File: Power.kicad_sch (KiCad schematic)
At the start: 30 parts

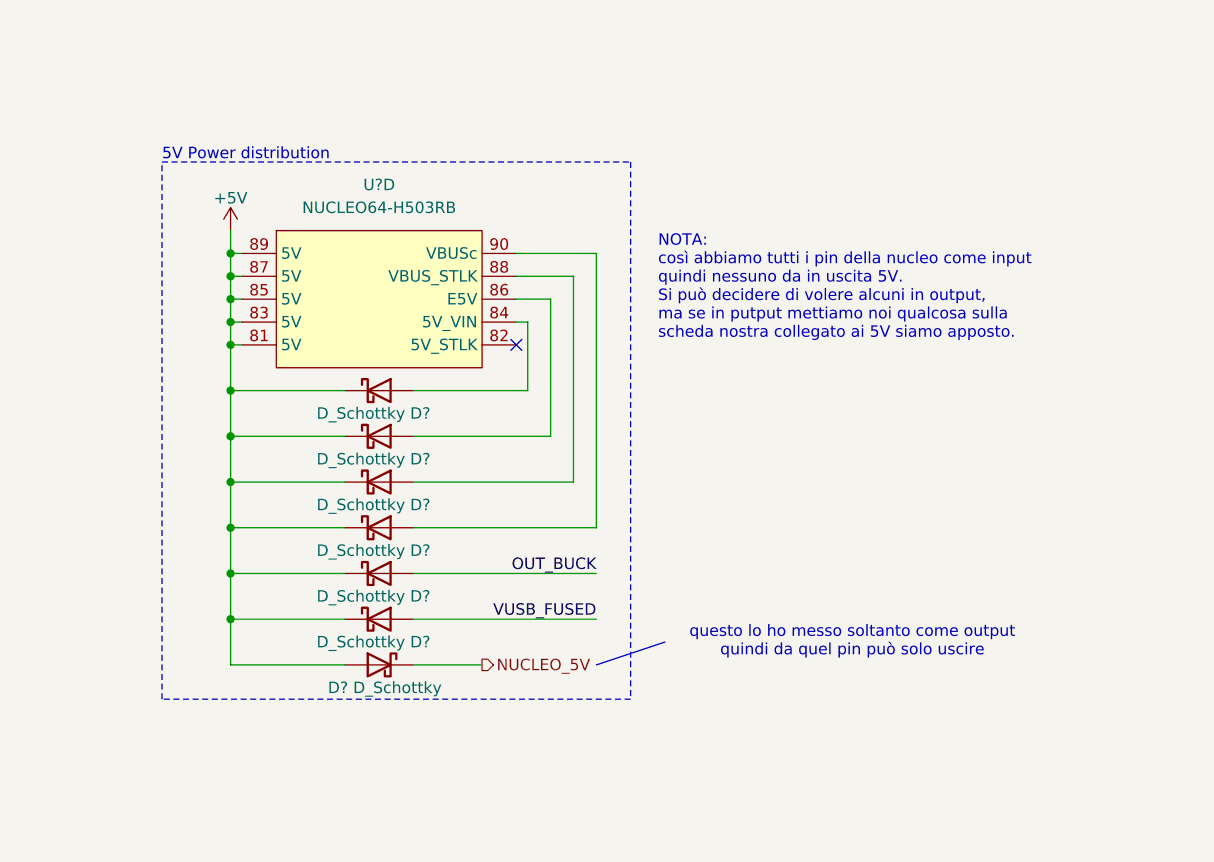
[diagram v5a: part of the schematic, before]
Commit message: Changed the grounding of the opto-coupled power stage + Added UI connectors + Removed a Diode on the Power Sheet (Fixes #3)
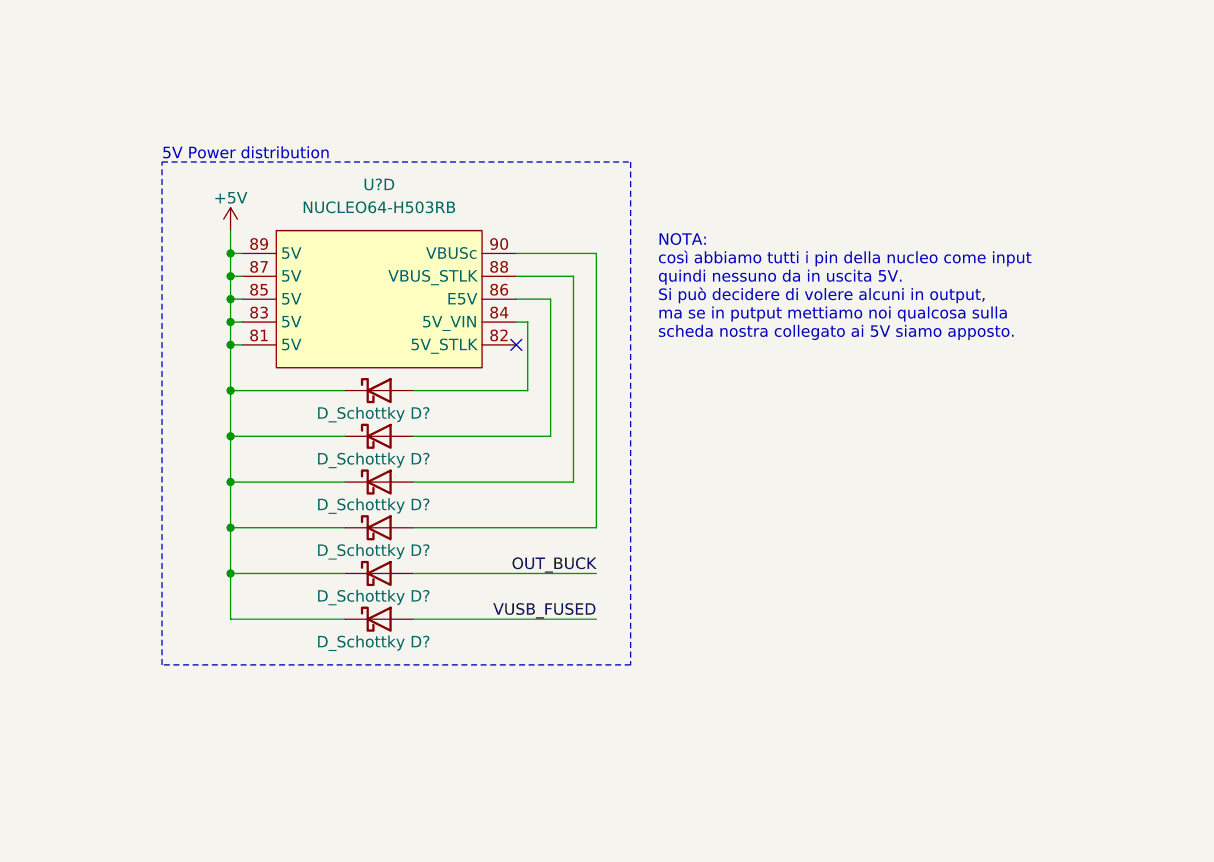
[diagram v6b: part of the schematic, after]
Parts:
- removed D?: D_Schottky, symbol Device:D_Schottky
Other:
- note removed: "questo lo ho messo soltanto come output quindi da quel pin può solo uscire"
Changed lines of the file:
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@@
 	(rectangle
 		(start 180.34 102.87)
-		(end 232.41 162.56)
+		(end 232.41 158.75)
 		(stroke
 			(width 0)
@@
 		)
 	)
-	(text "questo lo ho messo soltanto come output\nquindi da quel pin può solo uscire"
-		(exclude_from_sim no)
-		(at 257.048 156.21 0)
-		(effects
-			(font
-				(size 1.27 1.27)
-			)
-		)
-	)
 	(text "5V Power distribution"
 		(exclude_from_sim no)
@@
 	)
 	(junction
-		(at 187.96 153.67)
-		(diameter 0)
-		(color 0 0 0 0)
-	)
-	(junction
 		(at 161.29 33.02)
 		(diameter 0)
@@
 	(wire
 		(pts
-			(xy 208.28 158.75) (xy 215.9 158.75)
-		)
-		(stroke
-			(width 0)
-			(type default)
-		)
-	)
-	(wire
-		(pts
 			(xy 46.99 167.64) (xy 46.99 165.1)
 		)
@@
 	(wire
 		(pts
-			(xy 200.66 158.75) (xy 187.96 158.75)
-		)
-		(stroke
-			(width 0)
-			(type default)
-		)
-	)
-	(wire
-		(pts
 			(xy 95.25 41.91) (xy 95.25 43.18)
 		)
@@
 	(wire
 		(pts
+			(xy 219.71 115.57) (xy 226.06 115.57)
+		)
+		(stroke
+			(width 0)
+			(type default)
+		)
+	)
+	(wire
+		(pts
 			(xy 187.96 133.35) (xy 200.66 133.35)
 		)
@@
 	(wire
 		(pts
-			(xy 219.71 115.57) (xy 226.06 115.57)
-		)
-		(stroke
-			(width 0)
-			(type default)
-		)
-	)
-	(wire
-		(pts
 			(xy 191.77 33.02) (xy 207.01 33.02)
 		)
@@
 	(wire
 		(pts
-			(xy 187.96 158.75) (xy 187.96 153.67)
-		)
-		(stroke
-			(width 0)
-			(type default)
-		)
-	)
-	(wire
-		(pts
 			(xy 95.25 44.45) (xy 95.25 43.18)
 		)
@@
 		)
 	)
-	(polyline
-		(pts
-			(xy 228.6 158.75) (xy 236.22 156.21)
-		)
-		(stroke
-			(width 0)
-			(type default)
-		)
-	)
 	(wire
 		(pts
@@
 		)
 	)
-	(hierarchical_label "NUCLEO_5V"
-		(shape output)
-		(at 215.9 158.75 0)
-		(effects
-			(font
-				(size 1.27 1.27)
-			)
-			(justify left)
-		)
-	)
 	(hierarchical_label "NUCLEO_3V3"
 		(shape input)
@@
 	)
 	(symbol
-		(lib_id "Device:D_Schottky")
-		(at 204.47 158.75 0)
-		(mirror y)
-		(unit 1)
-		(exclude_from_sim no)
-		(in_bom yes)
-		(on_board yes)
-		(dnp no)
-		(property "Reference" "D?"
-			(at 199.898 161.29 0)
-			(effects
-				(font
-					(size 1.27 1.27)
-				)
-			)
-		)
-		(property "Value" "D_Schottky"
-			(at 206.502 161.29 0)
-			(effects
-				(font
-					(size 1.27 1.27)
-				)
-			)
-		)
-		(property "Footprint" ""
-			(at 204.47 158.75 0)
-			(effects
-				(font
-					(size 1.27 1.27)
-				)
-				(hide yes)
-			)
-		)
-		(property "Datasheet" "~"
-			(at 204.47 158.75 0)
-			(effects
-				(font
-					(size 1.27 1.27)
-				)
-				(hide yes)
-			)
-		)
-		(property "Description" "Schottky diode"
-			(at 204.47 158.75 0)
-			(effects
-				(font
-					(size 1.27 1.27)
-				)
-				(hide yes)
-			)
-		)
-		(pin "2"
-		)
-		(pin "1"
-		)
-		(instances
-			(project "Educational-Board_MainBoard"
-				(path "/835b4df9-7d62-45f4-81d2-5a64fbc86f3c/a1b70c1b-93fd-432d-b3bf-990581065c7c"
-					(reference "D?")
-					(unit 1)
-				)
-			)
-		)
-	)
-	(symbol
 		(lib_id "power:GND")
 		(at 238.76 46.99 0)
@@
 		(dnp no)
 		(fields_autoplaced yes)
-		(property "Reference" "#PWR030"
+		(property "Reference" "#PWR?"
 			(at 187.96 114.3 0)
 			(effects
@@
 			(project "Educational-Board_MainBoard"
 				(path "/835b4df9-7d62-45f4-81d2-5a64fbc86f3c/a1b70c1b-93fd-432d-b3bf-990581065c7c"
-					(reference "#PWR030")
+					(reference "#PWR?")
 					(unit 1)
 				)

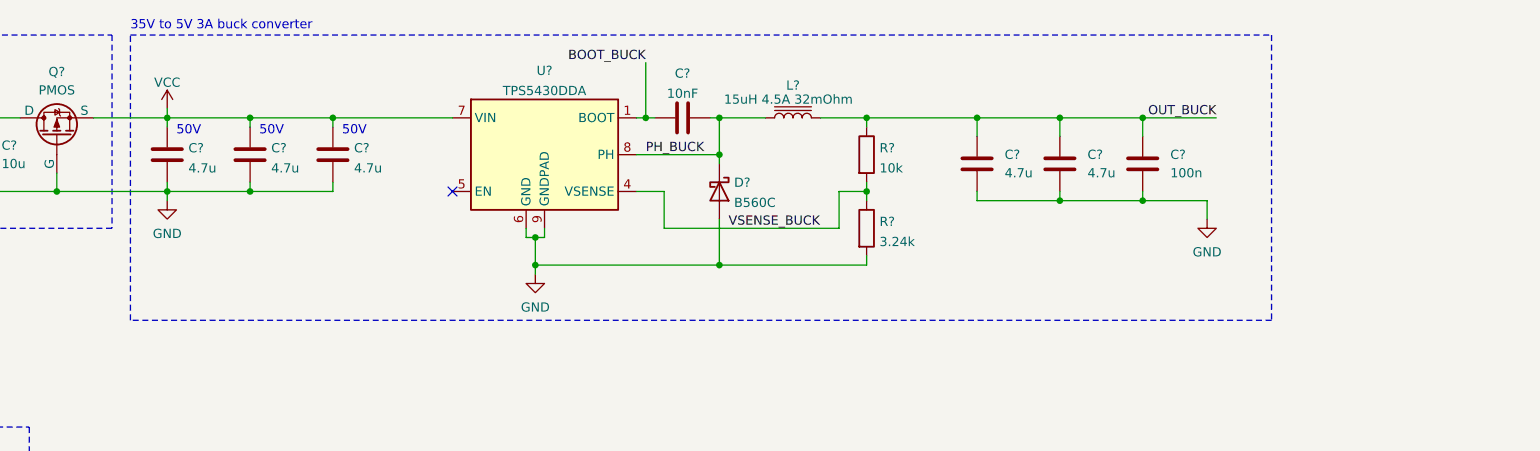
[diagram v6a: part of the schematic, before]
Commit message: Completated the Power Schema + Added Shunts resistors with OP Amp + Connected the RGB Connector to the BUCK (Fixes #5)
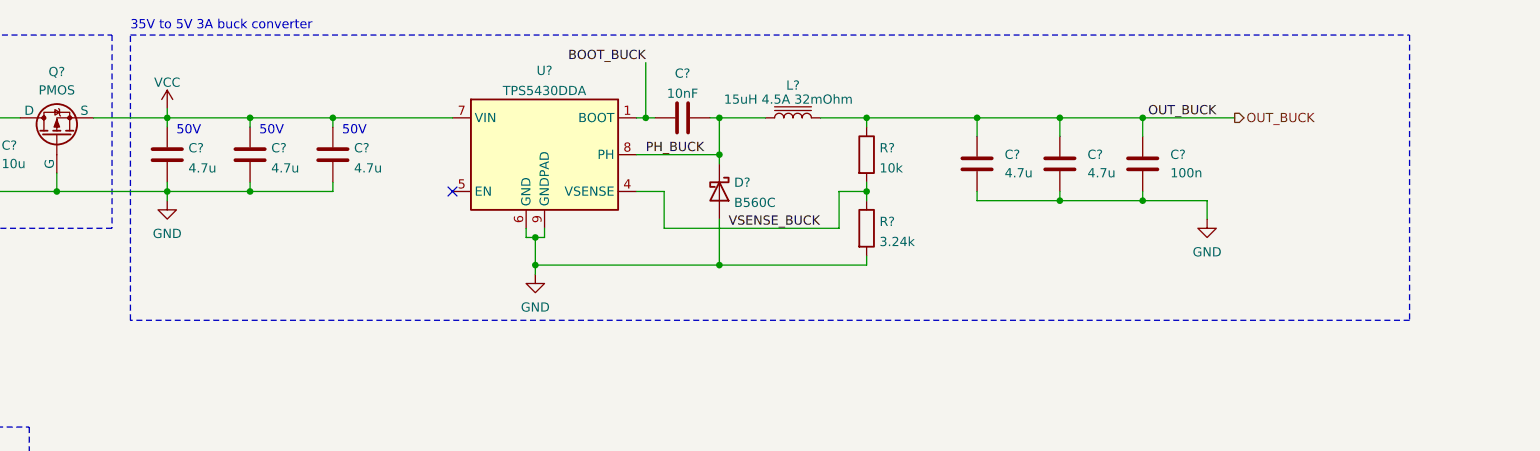
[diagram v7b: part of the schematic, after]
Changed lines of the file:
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@@
 	(rectangle
 		(start 90.17 21.59)
-		(end 247.65 60.96)
+		(end 266.7 60.96)
 		(stroke
 			(width 0)
@@
 	(wire
 		(pts
-			(xy 240.03 33.02) (xy 229.87 33.02)
+			(xy 229.87 33.02) (xy 242.57 33.02)
 		)
 		(stroke
@@
 		)
 	)
+	(hierarchical_label "OUT_BUCK"
+		(shape output)
+		(at 242.57 33.02 0)
+		(effects
+			(font
+				(size 1.27 1.27)
+			)
+			(justify left)
+		)
+	)
 	(hierarchical_label "NUCLEO_VDD"
 		(shape input)
@@
 		(dnp no)
 		(fields_autoplaced yes)
-		(property "Reference" "#PWR?"
+		(property "Reference" "#PWR0106"
 			(at 50.8 87.63 0)
 			(effects
@@
 			(project ""
 				(path "/835b4df9-7d62-45f4-81d2-5a64fbc86f3c/a1b70c1b-93fd-432d-b3bf-990581065c7c"
-					(reference "#PWR?")
+					(reference "#PWR0106")
 					(unit 1)
 				)
@@
 		(dnp no)
 		(fields_autoplaced yes)
-		(property "Reference" "#PWR?"
+		(property "Reference" "#PWR0107"
 			(at 85.09 161.29 0)
 			(effects
@@
 			(project "Educational-Board_MainBoard"
 				(path "/835b4df9-7d62-45f4-81d2-5a64fbc86f3c/a1b70c1b-93fd-432d-b3bf-990581065c7c"
-					(reference "#PWR?")
+					(reference "#PWR0107")
 					(unit 1)
 				)
@@
 		(dnp no)
 		(fields_autoplaced yes)
-		(property "Reference" "#PWR?"
+		(property "Reference" "#PWR0104"
 			(at 238.76 53.34 0)
 			(effects
@@
 			(project "Educational-Board_MainBoard"
 				(path "/835b4df9-7d62-45f4-81d2-5a64fbc86f3c/a1b70c1b-93fd-432d-b3bf-990581065c7c"
-					(reference "#PWR?")
+					(reference "#PWR0104")
 					(unit 1)
 				)
@@
 		(dnp no)
 		(fields_autoplaced yes)
-		(property "Reference" "#PWR?"
+		(property "Reference" "#PWR0105"
 			(at 187.96 114.3 0)
 			(effects
@@
 			(project "Educational-Board_MainBoard"
 				(path "/835b4df9-7d62-45f4-81d2-5a64fbc86f3c/a1b70c1b-93fd-432d-b3bf-990581065c7c"
-					(reference "#PWR?")
+					(reference "#PWR0105")
 					(unit 1)
 				)
@@
 		(dnp no)
 		(fields_autoplaced yes)
-		(property "Reference" "#PWR?"
+		(property "Reference" "#PWR0110"
 			(at 33.02 190.5 0)
 			(effects
@@
 			(project "Educational-Board_MainBoard"
 				(path "/835b4df9-7d62-45f4-81d2-5a64fbc86f3c/a1b70c1b-93fd-432d-b3bf-990581065c7c"
-					(reference "#PWR?")
+					(reference "#PWR0110")
 					(unit 1)
 				)
@@
 		(dnp no)
 		(fields_autoplaced yes)
-		(property "Reference" "#PWR?"
+		(property "Reference" "#PWR0109"
 			(at 62.23 171.45 0)
 			(effects
@@
 			(project "Educational-Board_MainBoard"
 				(path "/835b4df9-7d62-45f4-81d2-5a64fbc86f3c/a1b70c1b-93fd-432d-b3bf-990581065c7c"
-					(reference "#PWR?")
+					(reference "#PWR0109")
 					(unit 1)
 				)
@@
 		(dnp no)
 		(fields_autoplaced yes)
-		(property "Reference" "#PWR?"
+		(property "Reference" "#PWR0101"
 			(at 146.05 60.96 0)
 			(effects
@@
 			(project "Educational-Board_MainBoard"
 				(path "/835b4df9-7d62-45f4-81d2-5a64fbc86f3c/a1b70c1b-93fd-432d-b3bf-990581065c7c"
-					(reference "#PWR?")
+					(reference "#PWR0101")
 					(unit 1)
 				)
@@
 		(dnp no)
 		(fields_autoplaced yes)
-		(property "Reference" "#PWR?"
+		(property "Reference" "#PWR0103"
 			(at 95.25 35.56 0)
 			(effects
@@
 			(project "Educational-Board_MainBoard"
 				(path "/835b4df9-7d62-45f4-81d2-5a64fbc86f3c/a1b70c1b-93fd-432d-b3bf-990581065c7c"
-					(reference "#PWR?")
+					(reference "#PWR0103")
 					(unit 1)
 				)
@@
 		(dnp no)
 		(fields_autoplaced yes)
-		(property "Reference" "#PWR?"
+		(property "Reference" "#PWR0102"
 			(at 95.25 50.8 0)
 			(effects
@@
 			(project "Educational-Board_MainBoard"
 				(path "/835b4df9-7d62-45f4-81d2-5a64fbc86f3c/a1b70c1b-93fd-432d-b3bf-990581065c7c"
-					(reference "#PWR?")
+					(reference "#PWR0102")
 					(unit 1)
 				)
@@
 		(dnp no)
 		(fields_autoplaced yes)
-		(property "Reference" "#PWR?"
+		(property "Reference" "#PWR0108"
 			(at 74.93 161.29 0)
 			(effects
@@
 			(project "Educational-Board_MainBoard"
 				(path "/835b4df9-7d62-45f4-81d2-5a64fbc86f3c/a1b70c1b-93fd-432d-b3bf-990581065c7c"
-					(reference "#PWR?")
+					(reference "#PWR0108")
 					(unit 1)
 				)
@@
 		(dnp no)
 		(fields_autoplaced yes)
-		(property "Reference" "#FLG?"
+		(property "Reference" "#FLG0101"
 			(at 69.85 141.605 0)
 			(effects
@@
 			(project "Educational-Board_MainBoard"
 				(path "/835b4df9-7d62-45f4-81d2-5a64fbc86f3c/a1b70c1b-93fd-432d-b3bf-990581065c7c"
-					(reference "#FLG?")
+					(reference "#FLG0101")
 					(unit 1)
 				)

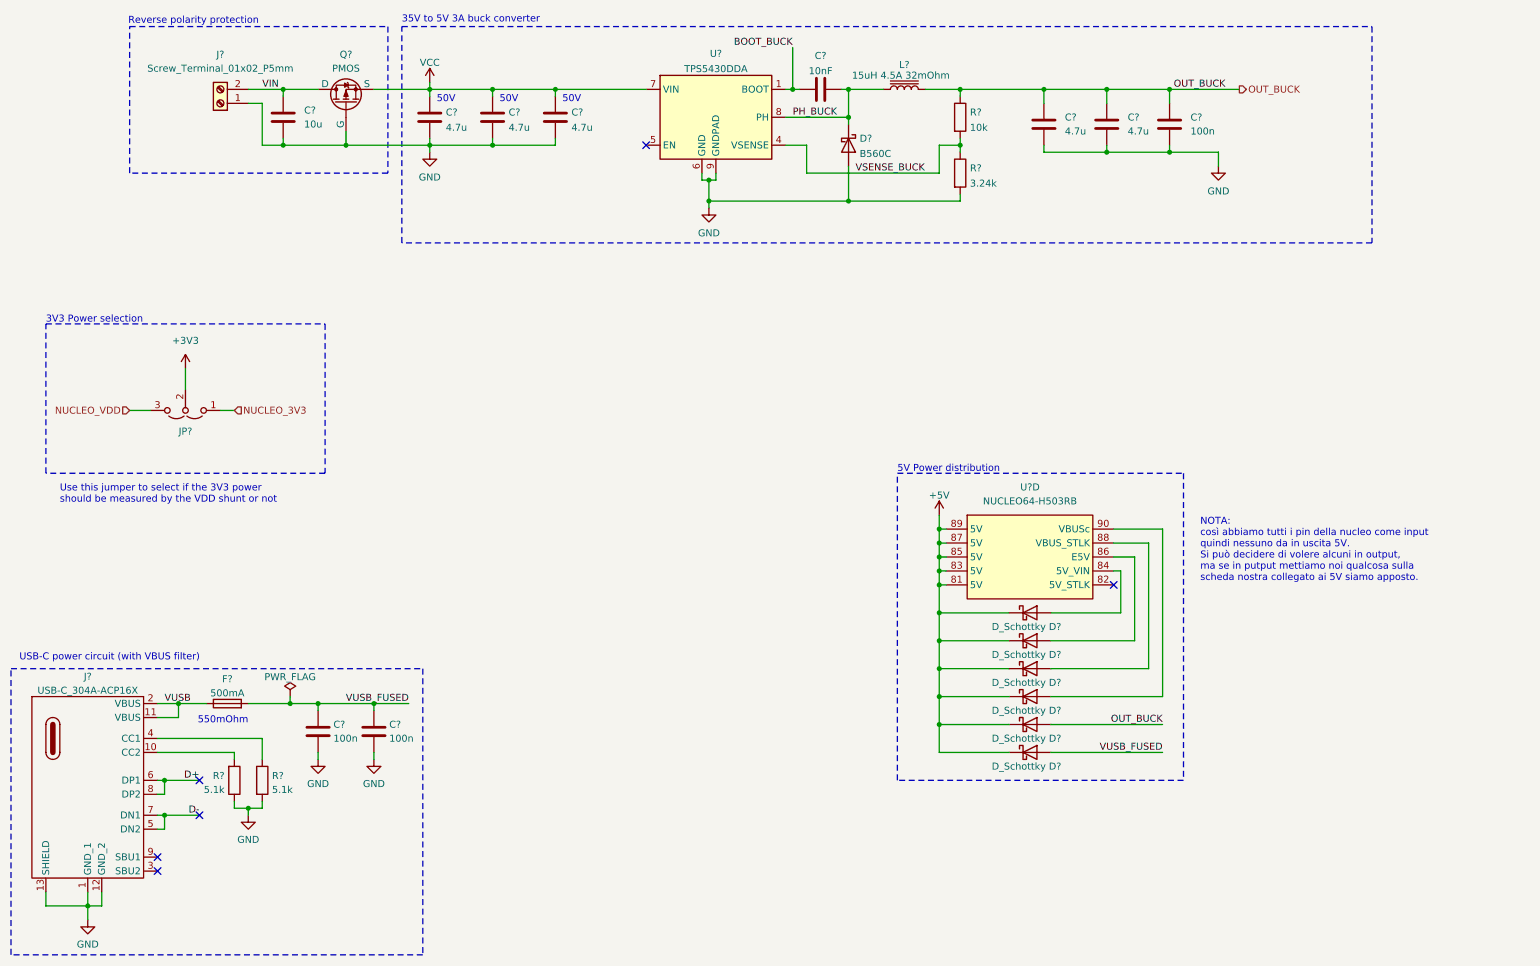
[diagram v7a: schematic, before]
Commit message: Runned ERC for the first time and fixed some errors
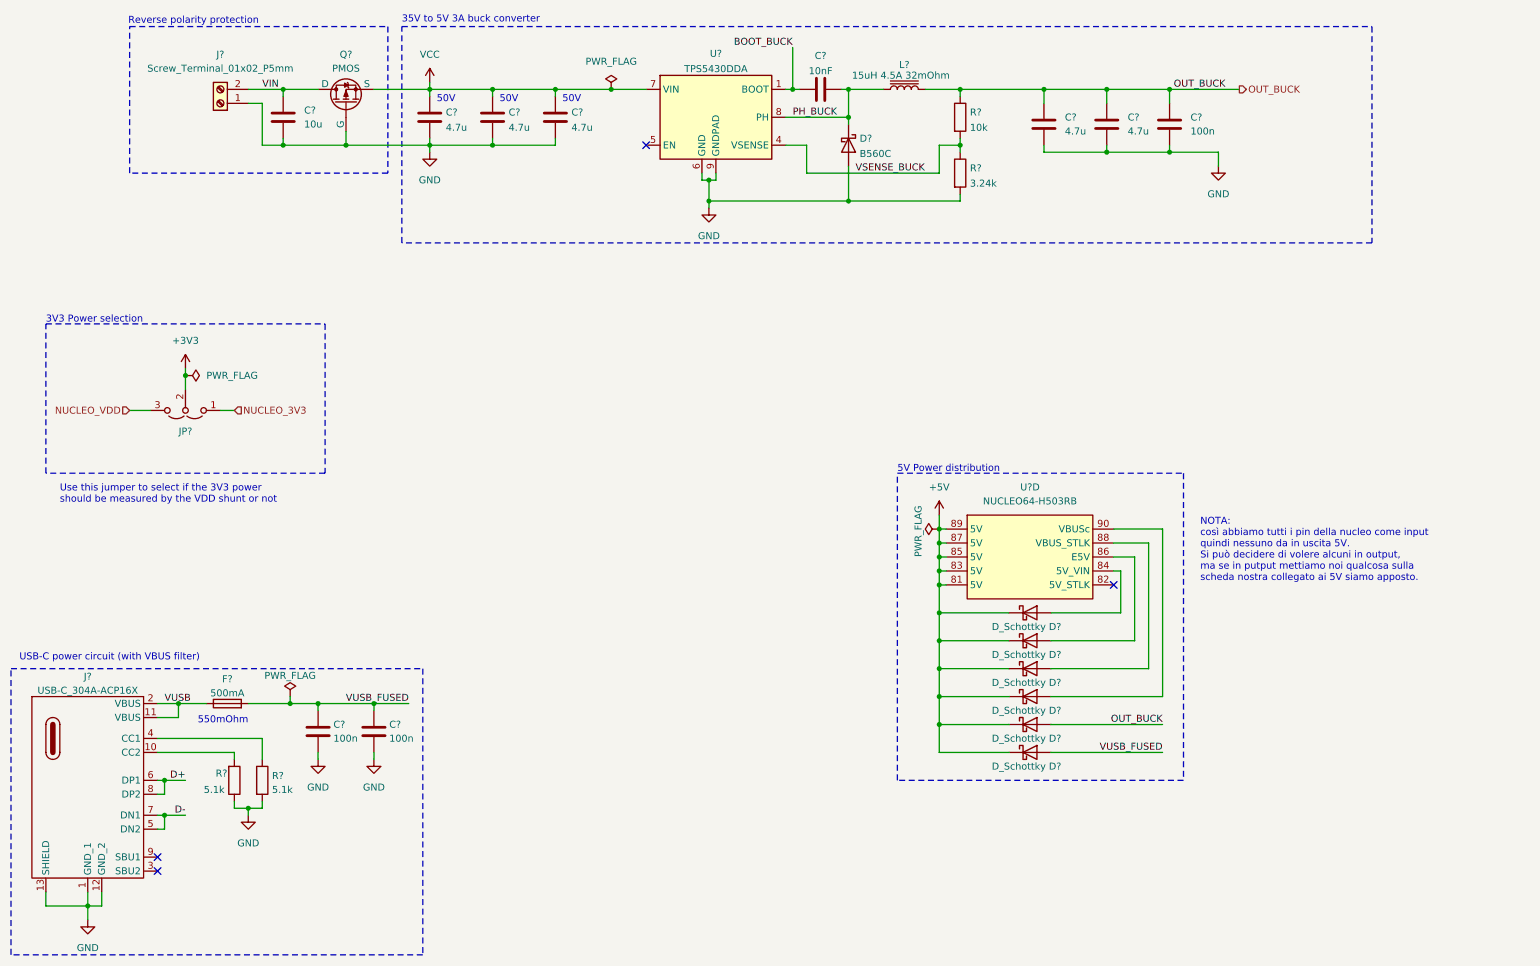
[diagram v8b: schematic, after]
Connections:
- no-connect marks 6 -> 4
